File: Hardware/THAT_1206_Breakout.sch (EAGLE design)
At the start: 31 parts, among them IC1 THAT1206, J1 INPUT, J2 CHASSIS, J3 RN, J4 TN, J5 SN, J6 1x4, J7 R, J8 T

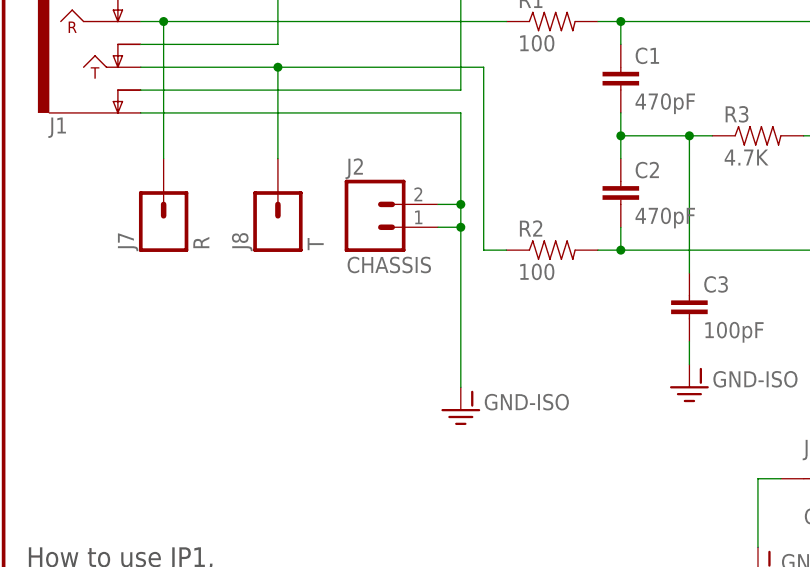
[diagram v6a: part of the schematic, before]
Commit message: Updates after group review.
-Chassis ground moved out of selective solder runout path.
-Flame turned right side up.
-A few via/silk overlaps fixed.
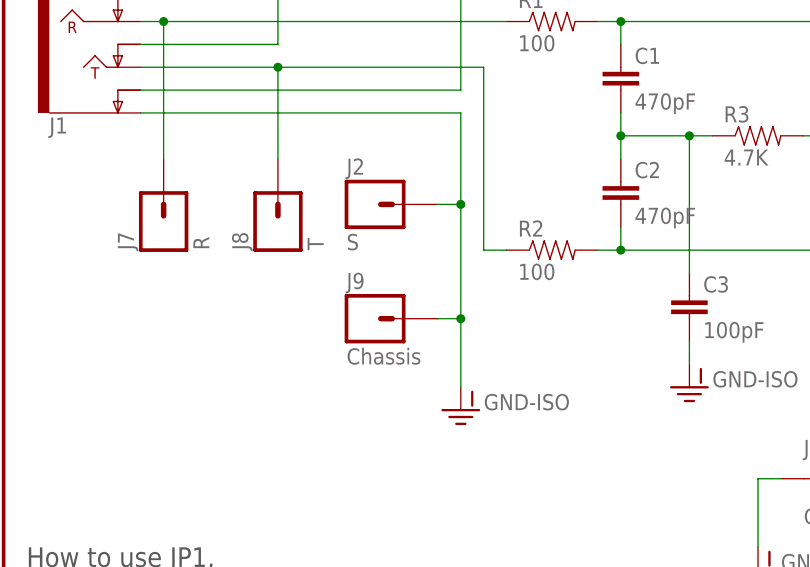
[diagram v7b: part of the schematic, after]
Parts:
- added J9: Chassis, SparkFun-Connectors:M01PTH_NO_SILK_YES_STOP
- J2: value CHASSIS -> S; device SparkFun-Connectors:M021X02_NO_SILK -> SparkFun-Connectors:M01PTH_NO_SILK_YES_STOP
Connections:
- net GND-ISO: now also J9.1; no longer J2.2
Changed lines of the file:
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@@
 <part name="GND4" library="SparkFun-Aesthetics" deviceset="GND" device=""/>
 <part name="GND2" library="SparkFun-Aesthetics" deviceset="GND" device=""/>
-<part name="J2" library="SparkFun-Connectors" deviceset="M02" device="1X02_NO_SILK" value="CHASSIS"/>
 <part name="SUPPLY4" library="SparkFun-Aesthetics" deviceset="VCC" device=""/>
 <part name="SUPPLY1" library="SparkFun-Aesthetics" deviceset="VNEG" device=""/>
@@
 <part name="J7" library="SparkFun-Connectors" deviceset="M01" device="PTH_NO_SILK_YES_STOP" value="R"/>
 <part name="J8" library="SparkFun-Connectors" deviceset="M01" device="PTH_NO_SILK_YES_STOP" value="T"/>
+<part name="J2" library="SparkFun-Connectors" deviceset="M01" device="PTH_NO_SILK_YES_STOP" value="S"/>
+<part name="J9" library="SparkFun-Connectors" deviceset="M01" device="PTH_NO_SILK_YES_STOP" value="Chassis"/>
 </parts>
 <sheets>
@@
 <instance part="GND4" gate="1" x="165.1" y="71.12"/>
 <instance part="GND2" gate="1" x="144.78" y="73.66"/>
-<instance part="J2" gate="G$1" x="40.64" y="81.28"/>
 <instance part="SUPPLY4" gate="G$1" x="167.64" y="137.16"/>
 <instance part="SUPPLY1" gate="G$2" x="81.28" y="119.38"/>
@@
 <instance part="J7" gate="G$1" x="17.78" y="81.28" rot="R90"/>
 <instance part="J8" gate="G$1" x="30.48" y="81.28" rot="R90"/>
+<instance part="J2" gate="G$1" x="40.64" y="83.82"/>
+<instance part="J9" gate="G$1" x="40.64" y="71.12"/>
 </instances>
 <busses>
@@
 <segment>
 <pinref part="GND-ISO1" gate="G$1" pin="GND-ISO"/>
-<wire x1="50.8" y1="63.5" x2="50.8" y2="81.28" width="0.1524" layer="91"/>
+<wire x1="50.8" y1="63.5" x2="50.8" y2="71.12" width="0.1524" layer="91"/>
 <pinref part="J1" gate="G$1" pin="EARTH"/>
-<wire x1="50.8" y1="81.28" x2="50.8" y2="83.82" width="0.1524" layer="91"/>
+<wire x1="50.8" y1="71.12" x2="50.8" y2="83.82" width="0.1524" layer="91"/>
 <wire x1="50.8" y1="83.82" x2="50.8" y2="93.98" width="0.1524" layer="91"/>
 <wire x1="15.24" y1="93.98" x2="50.8" y2="93.98" width="0.1524" layer="91"/>
-<pinref part="J2" gate="G$1" pin="2"/>
 <wire x1="48.26" y1="83.82" x2="50.8" y2="83.82" width="0.1524" layer="91"/>
+<wire x1="48.26" y1="71.12" x2="50.8" y2="71.12" width="0.1524" layer="91"/>
+<junction x="50.8" y="71.12"/>
+<junction x="50.8" y="83.82"/>
 <pinref part="J2" gate="G$1" pin="1"/>
-<wire x1="48.26" y1="81.28" x2="50.8" y2="81.28" width="0.1524" layer="91"/>
-<junction x="50.8" y="81.28"/>
-<junction x="50.8" y="83.82"/>
-</segment>
-</net>
+<pinref part="J9" gate="G$1" pin="1"/>
+</segment>
+</net>

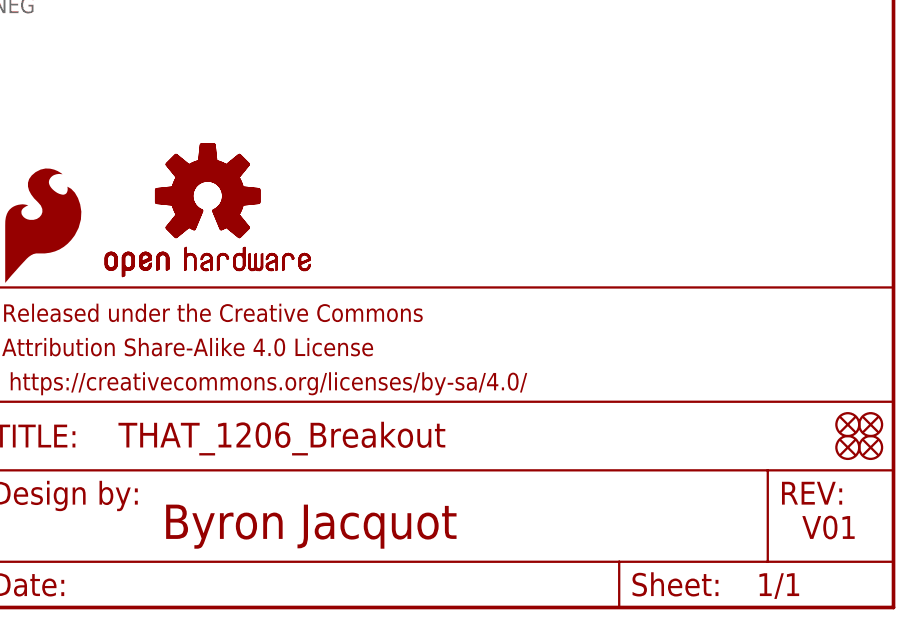
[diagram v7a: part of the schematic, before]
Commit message: Updated after running checklist.
Biggest change is that TRS jack was updated with new libraries.
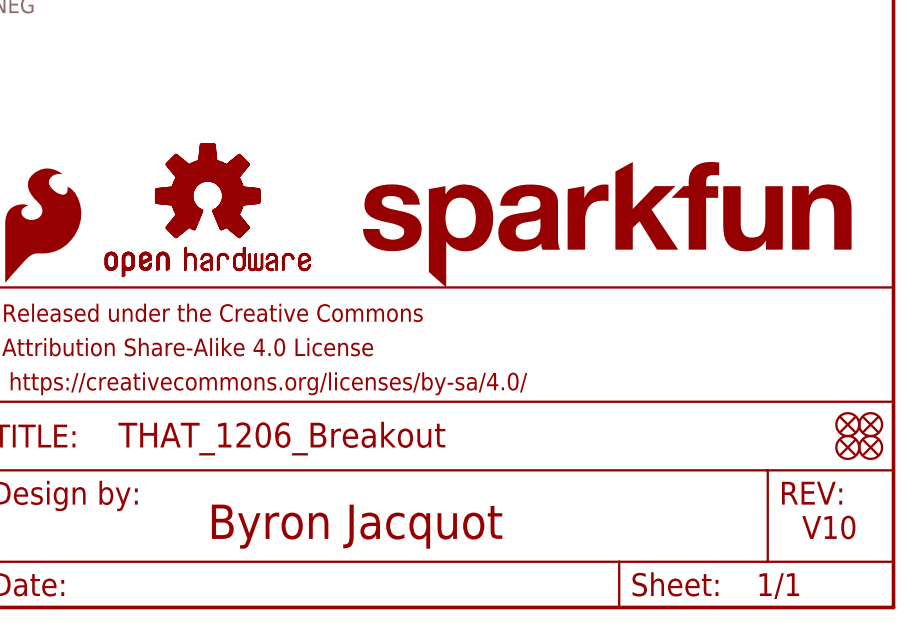
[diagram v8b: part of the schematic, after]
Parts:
- added LOGO5: SFE_LOGO_NAME.1_INCH, SparkFun-Aesthetics:SFE_LOGO_NAME.1_INCH
- J1: device SparkFun-Connectors:AUDIO-JACK4-.25-HORIZ-TRS -> SparkFun-Connectors:AUDIO_JACK_TRS_0.25"_PTH_RA
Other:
- note added: "V10"
- note removed: "V01"
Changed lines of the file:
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@@
 <parts>
 <part name="FRAME1" library="SparkFun-Aesthetics" deviceset="FRAME-LETTER" device=""/>
-<part name="J1" library="SparkFun-Connectors" deviceset="AUDIO-JACK4-.25-HORIZ-TRS" device="" value="INPUT"/>
+<part name="J1" library="SparkFun-Connectors" deviceset="AUDIO_JACK_TRS_0.25&quot;_PTH_RA" device="" value="INPUT"/>
 <part name="SUPPLY2" library="SparkFun-Aesthetics" deviceset="VCC" device=""/>
 <part name="GND-ISO1" library="SparkFun-Aesthetics" deviceset="GND-ISO" device=""/>
@@
 <part name="FD4" library="SparkFun-Aesthetics" deviceset="FIDUCIAL" device="UFIDUCIAL"/>
 <part name="LOGO2" library="SparkFun-Aesthetics" deviceset="SFE_LOGO_FLAME" device=".2_INCH" value="SFE_LOGO_FLAME.2_INCH"/>
-<part name="FD1" library="SparkFun-Aesthetics" deviceset="FIDUCIAL" device="UFIDUCIAL"/>
-<part name="FD2" library="SparkFun-Aesthetics" deviceset="FIDUCIAL" device="UFIDUCIAL"/>
 <part name="J3" library="SparkFun-Connectors" deviceset="M01" device="PTH_NO_SILK_YES_STOP" value="RN"/>
 <part name="J4" library="SparkFun-Connectors" deviceset="M01" device="PTH_NO_SILK_YES_STOP" value="TN"/>
@@
 <part name="J2" library="SparkFun-Connectors" deviceset="M01" device="PTH_NO_SILK_YES_STOP" value="S"/>
 <part name="J9" library="SparkFun-Connectors" deviceset="M01" device="PTH_NO_SILK_YES_STOP" value="Chassis"/>
+<part name="LOGO5" library="SparkFun-Aesthetics" deviceset="SFE_LOGO_NAME" device=".1_INCH"/>
+<part name="FD1" library="SparkFun-Aesthetics" deviceset="FIDUCIAL" device="UFIDUCIAL"/>
+<part name="FD2" library="SparkFun-Aesthetics" deviceset="FIDUCIAL" device="UFIDUCIAL"/>
 </parts>
 <sheets>
 <sheet>
 <plain>
-<text x="167.64" y="7.62" size="3.81" layer="94" font="vector">Byron Jacquot</text>
-<text x="238.76" y="7.62" size="2.54" layer="94" font="vector">V01</text>
+<text x="172.72" y="7.62" size="3.81" layer="94" font="vector">Byron Jacquot</text>
+<text x="238.76" y="7.62" size="2.54" layer="94" font="vector">V10</text>
 <text x="2.54" y="45.72" size="2.1844" layer="97" font="vector" align="top-left">How to use JP1,
 a note on grounding &amp; shielding:
@@
 <instance part="FD4" gate="G$1" x="246.38" y="17.78"/>
 <instance part="LOGO2" gate="G$1" x="149.86" y="35.56"/>
-<instance part="FD1" gate="G$1" x="243.84" y="20.32"/>
-<instance part="FD2" gate="G$1" x="243.84" y="17.78"/>
 <instance part="J3" gate="G$1" x="17.78" y="127" rot="R270"/>
 <instance part="J4" gate="G$1" x="30.48" y="127" rot="R270"/>
@@
 <instance part="J2" gate="G$1" x="40.64" y="83.82"/>
 <instance part="J9" gate="G$1" x="40.64" y="71.12"/>
+<instance part="LOGO5" gate="G$1" x="187.96" y="35.56"/>
+<instance part="FD1" gate="G$1" x="243.84" y="20.32"/>
+<instance part="FD2" gate="G$1" x="243.84" y="17.78"/>
 </instances>
 <busses>
